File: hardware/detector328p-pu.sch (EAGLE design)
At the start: 61 parts, among them J1 AVR_SPI_PRG_6NS, K1 SRD-05VDC-SL-C, Q1 BS170, Q2 16MHz, T1 BC337, T2 BC337, T3 BC337, U1 ATMEGA328P-AU

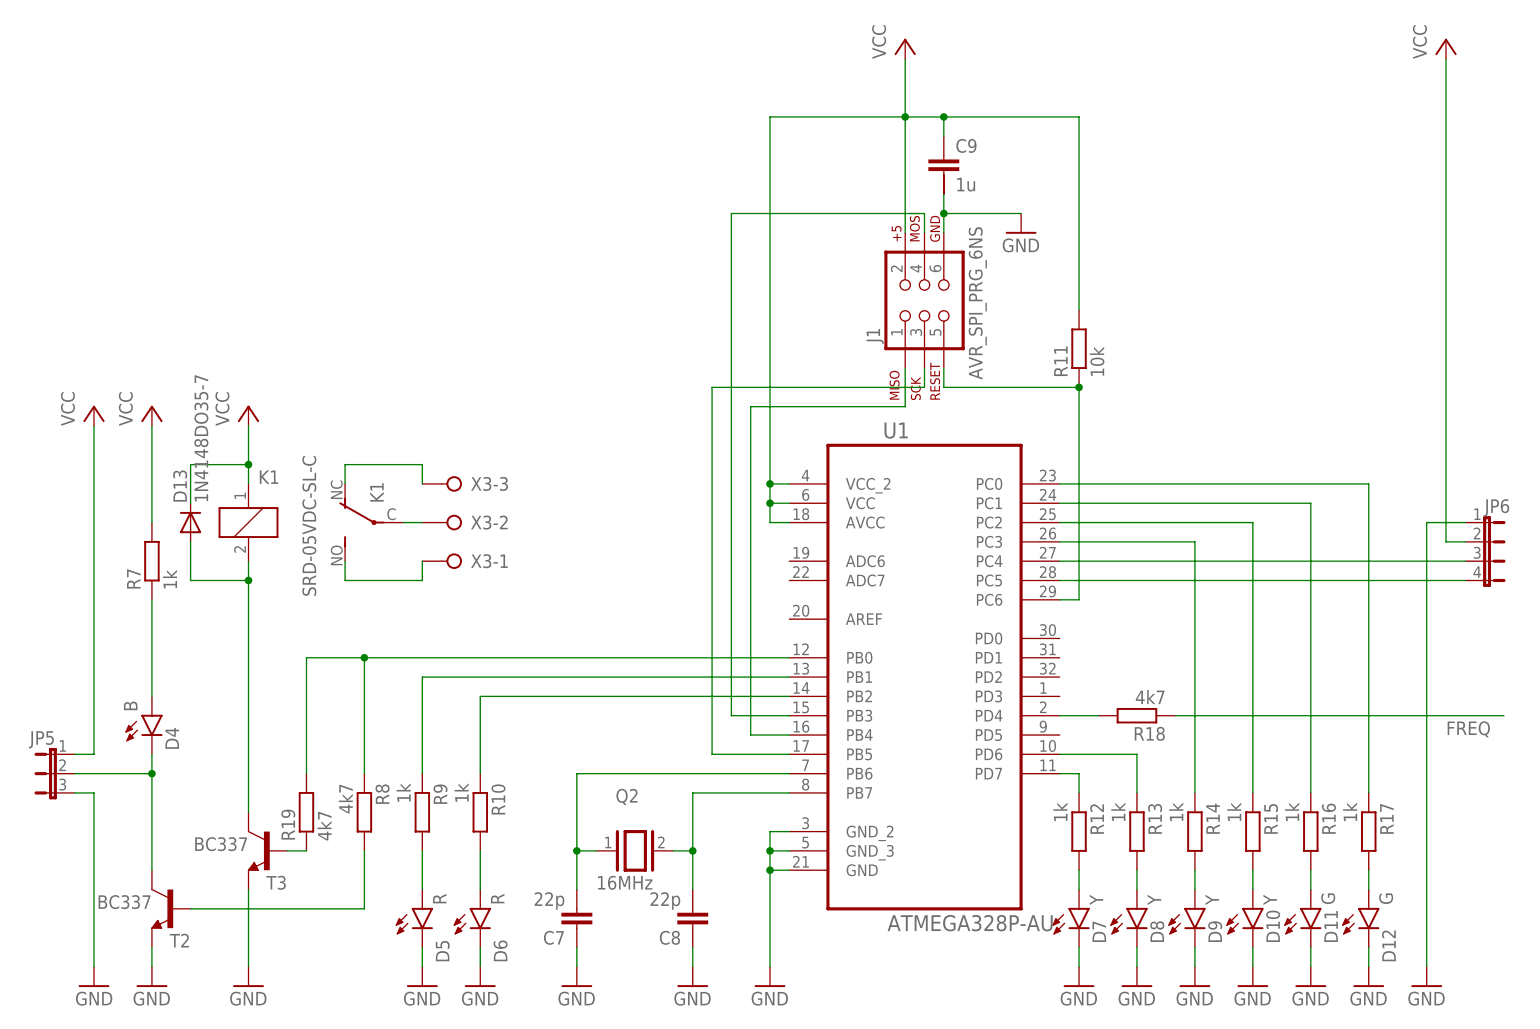
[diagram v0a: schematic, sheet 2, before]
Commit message: hardware: separate DIP and SIL drawings for mega328p, gitignore tuning
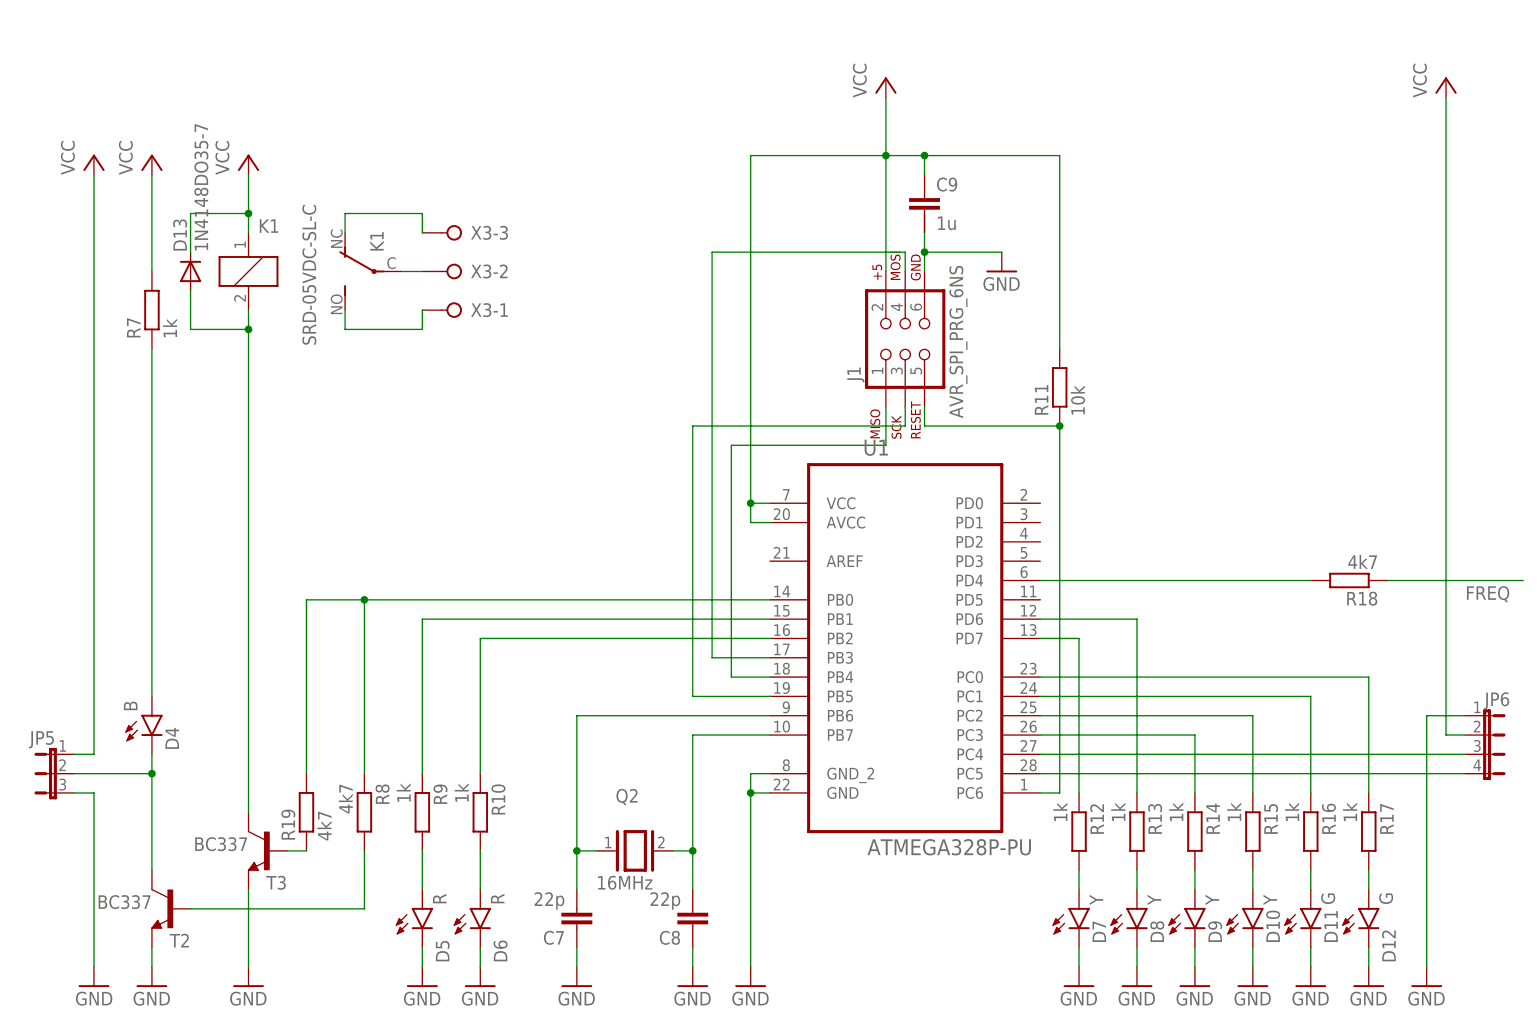
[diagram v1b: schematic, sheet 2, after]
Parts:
- U1: value ATMEGA328P-AU -> ATMEGA328P-PU; device Atmel_By_element14_Batch_1-00:ATMEGA328P-AU -> Atmel_By_element14_Batch_1-00:ATMEGA328P-PU
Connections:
- net GND: no longer U1.GND_3
- net VCC: no longer U1.VCC_2
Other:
- moved on the sheet: C9, D13, J1, JP6, K1, R11, R18, R7, X3-1, X3-2, X3-3

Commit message: hardware-m328p-pu: board created
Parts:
- removed JP2, JP3: (no value), SparkFun-Retired:JUMPER-2PTH
- added PB1, PB2: TACTILE-SWITCH-PTH, GeekAmmo:TACTILE-SWITCH-PTH
- added R20: 1k, resistor:R-EU_0204/5
- C1, C2, C3, C4, C7, C8: device resistor:C-EU050-024X044 -> resistor:C-EU025-025X050
- C5, C6, C9: device capacitor-wima:C-2.5-5/4 -> rcl:C-EU025-030X050
- D1, D2: device SparkFun-DiscreteSemi:DIODE-ZENER -> diode:ZENER-DIODEZD-5
- D13: value 1N4148DO35-7 -> (none); device diode:1N4148DO35-7 -> diode:DIODE-D-5
- JP1: device SparkFun-Retired:JUMPER-2PTH -> jumper:JP3QE
- Q1: value BS170 -> BS170.; device transistor-small-signal:BS170 -> detector:BS170.
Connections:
- new net N$47: GDT1.2, GDT2.1, L1.6, R1.2, X1-3.KL
- net GND: now also JP4-3.2, PB2.3, PB2.4; no longer C6.1, JP4-3.1, X2-1.KL
- net GND-ISO: now also X1-2.KL; no longer X1-3.KL
- net N$11: now also JP1-3.2; no longer JP1.1
- net N$14: now also L1.1; no longer L1.6
- net N$21: now also R20.2, U1.PB0; no longer GDT1.2, GDT2.1, L1.3, R1.2, X1-2.KL
- net N$38: now also PB1.1, PB1.2, R20.1; no longer U1.PB0
- net N$4: now also JP1-2.2; no longer JP2.1
- net N$41: now also X3-1.KL; no longer X3-3.KL
- net N$42: now also X3-3.KL; no longer X3-1.KL
- net N$44: now also PB2.1, PB2.2
- net N$5: now also JP1-1.2; no longer JP3.1
- net N$6: now also JP1-1.1, JP1-2.1, JP1-3.1, L1.3; no longer JP1.2, JP2.2, JP3.2, L1.4
- net N$7: now also L1.4; no longer L1.1
- net VCC: now also C6.1, JP4-3.1, PB1.3, PB1.4, X2-1.KL; no longer JP4-3.2
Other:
- moved on the sheet: GDT1, GDT2, R1, X1-1, X1-2, X1-3, X3-1, X3-2, X3-3
